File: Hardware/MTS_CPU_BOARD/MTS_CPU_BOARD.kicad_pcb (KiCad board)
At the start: 6 copper layers, 160 x 100 mm, 12 parts, among them J1 DIN41612_02x16_ZB, SW1 SW_DIP_x04, U1 TCAN337GDR, U3 24LC32

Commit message: Add some connectors
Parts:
- added C1: 100n, Capacitor_SMD:C_0402_1005Metric, F.Cu at (118.0, 107.2)
- added D1: Led1, LED_SMD:LED_0805_2012Metric, F.Cu at (198.8, 94.5)
- added J2: THD-02-R, Connector_PinHeader_2.54mm:PinHeader_2x02_P2.54mm_Vertical, F.Cu at (111.7, 108.5)
- added J3: HDMI_A_1.4, Connector_Video:HDMI_A_Kycon_KDMIX-SL1-NS-WS-B15_VerticalRightAngle, F.Cu at (89.9, 95.0)
- added J4: USB3_A_Stacked, Connector_USB:USB3_A_Molex_48406-0001_Horizontal_Stacked, F.Cu at (91.0, 74.0)
- added Module1: ComputeModule4-CM4, CM4IO:Raspberry-Pi-4-Compute-Module, F.Cu at (171.2, 60.0)
- added R1: 680R, Resistor_SMD:R_0805_2012Metric_Pad1.20x1.40mm_HandSolder, F.Cu at (198.9, 91.5)
- added R2: 470R, Resistor_SMD:R_0402_1005Metric, F.Cu at (116.7, 114.3)
- added R3: 470R, Resistor_SMD:R_0402_1005Metric, F.Cu at (116.7, 116.3)
- added S1: SWD, Connector_PinHeader_1.27mm:PinHeader_2x05_P1.27mm_Vertical_SMD, F.Cu at (191.8, 94.2)
- added U2: STM32G431K6Tx, Package_QFP:LQFP-32_7x7mm_P0.8mm, F.Cu at (192.2, 114.9)
- added U4: TPD4EUSB30, Package_SON:USON-10_2.5x1.0mm_P0.5mm, F.Cu at (110.9, 115.6)
- added U5: TPD4EUSB30, Package_SON:USON-10_2.5x1.0mm_P0.5mm, F.Cu at (113.8, 115.6)
- added U6: MagJack-A70-112-331N126, CM4IO:TRJG0926HENL, F.Cu at (90.8, 112.1)
- moved SW1 6.10 mm to (212.2, 114.2), turned to 0 degrees
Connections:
- net /CANH renamed /Conn/CANH
- net /CANL renamed /Conn/CANL
- net /I2C2_CLK_STM_CAN renamed /Conn/I2C2_CLK_STM_CAN
- net /I2C2_SDA_STM_CAN renamed /Conn/I2C2_SDA_STM_CAN
- net /Triger renamed /Conn/Triger

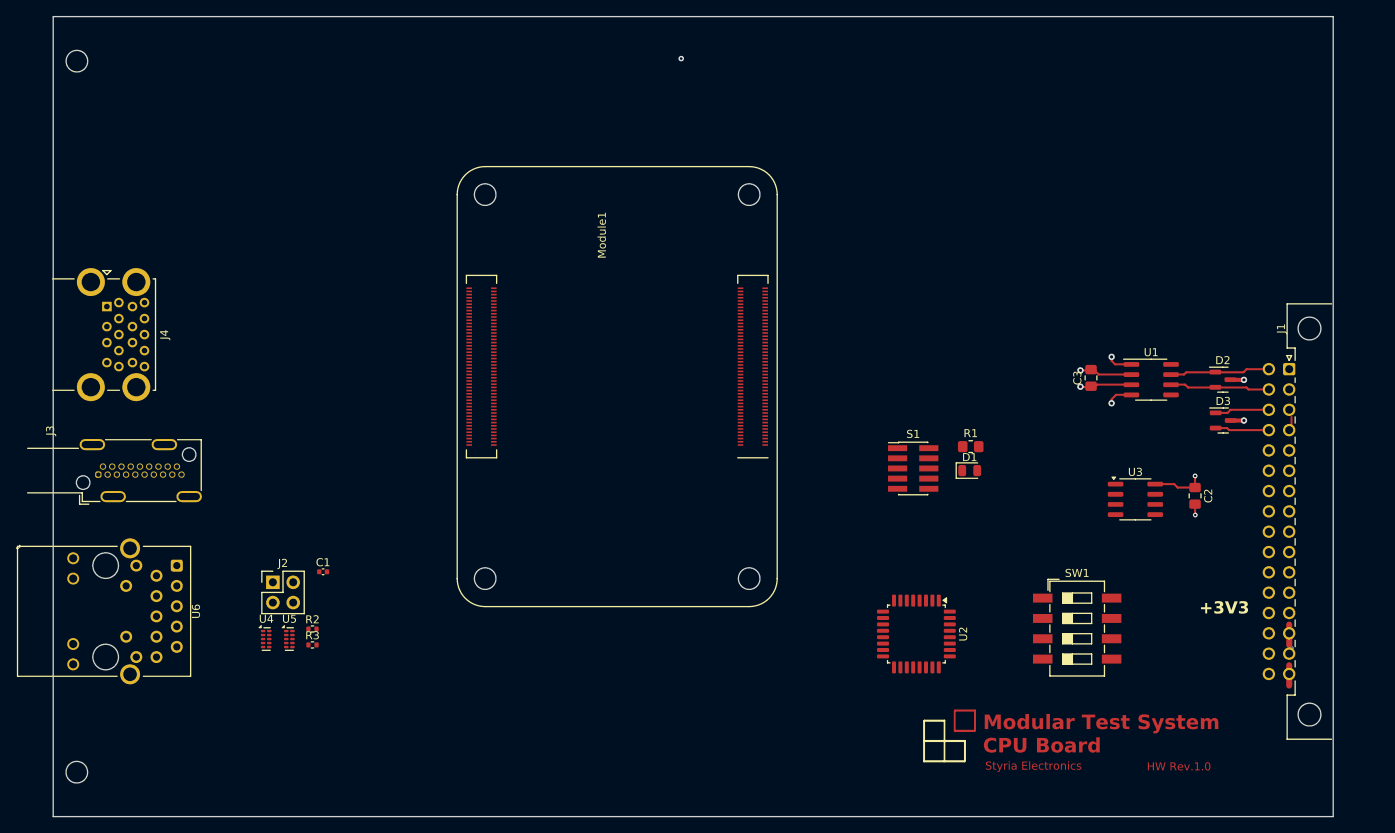
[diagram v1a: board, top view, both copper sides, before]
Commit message: Add EtherCAT
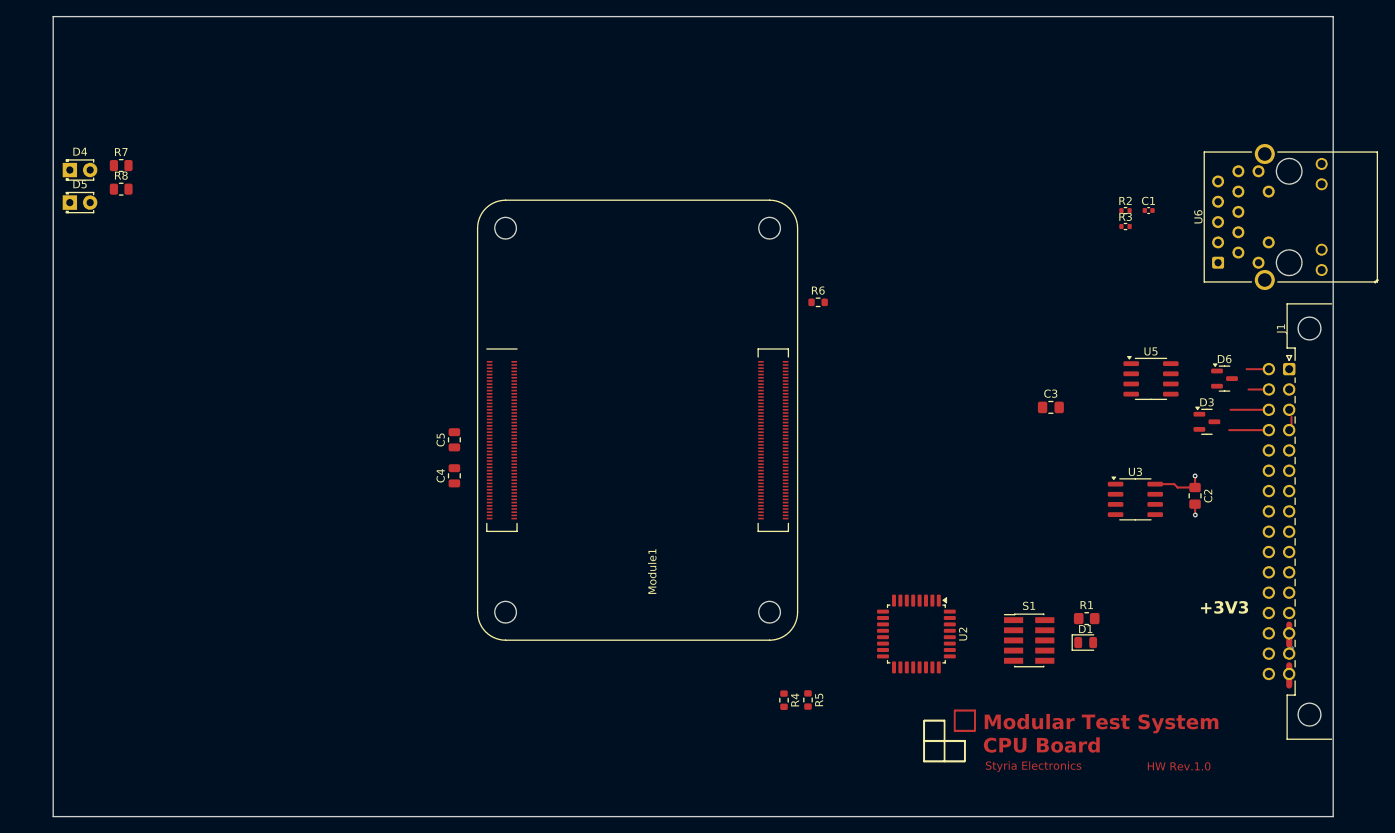
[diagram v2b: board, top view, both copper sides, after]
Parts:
- removed D2: PESD2CANFD24V-T, Package_TO_SOT_SMD:SOT-23
- removed J2: THD-02-R, Connector_PinHeader_2.54mm:PinHeader_2x02_P2.54mm_Vertical
- removed J3: HDMI_A_1.4, Connector_Video:HDMI_A_Kycon_KDMIX-SL1-NS-WS-B15_VerticalRightAngle
- removed J4: USB3_A_Stacked, Connector_USB:USB3_A_Molex_48406-0001_Horizontal_Stacked
- removed MH1, MH3: MountingHole_2.7mm_M2.5_DIN965, MountingHole:MountingHole_2.7mm_M2.5_DIN965
- removed SW1: SW_DIP_x04, Button_Switch_SMD:SW_DIP_SPSTx04_Slide_6.7x11.72mm_W8.61mm_P2.54mm_LowProfile
- removed U1: TCAN337GDR, Package_SO:SOIC-8_3.9x4.9mm_P1.27mm
- removed U4: TPD4EUSB30, Package_SON:USON-10_2.5x1.0mm_P0.5mm
- added C4: 10u, Capacitor_SMD:C_0805_2012Metric, F.Cu at (134.4, 95.2)
- added C5: 10u, Capacitor_SMD:C_0805_2012Metric, F.Cu at (134.4, 90.7)
- added D4: RED, LED_THT:LED_D1.8mm_W3.3mm_H2.4mm, F.Cu at (86.3, 56.9)
- added D5: GREEN, LED_THT:LED_D1.8mm_W3.3mm_H2.4mm, F.Cu at (86.3, 61.0)
- added D6: PESD2CANFD24V-T, Package_TO_SOT_SMD:SOT-23, F.Cu at (230.7, 83.0)
- added R4: 2K2, Resistor_SMD:R_0603_1608Metric, F.Cu at (175.6, 123.2)
- added R5: 2K2, Resistor_SMD:R_0603_1608Metric, F.Cu at (178.6, 123.2)
- added R6: 2.2K, Resistor_SMD:R_0603_1608Metric, F.Cu at (179.9, 73.5)
- added R7: 470R, Resistor_SMD:R_0805_2012Metric, F.Cu at (92.8, 56.4)
- added R8: 470R, Resistor_SMD:R_0805_2012Metric, F.Cu at (92.8, 59.3)
- U5: value TPD4EUSB30 -> TCAN337GDR; footprint Package_SON:USON-10_2.5x1.0mm_P0.5mm -> Package_SO:SOIC-8_3.9x4.9mm_P1.27mm
- moved U6 155.9 mm to (238.8, 62.8), turned to 90 degrees
- moved R2 114.3 mm to (218.3, 62.0)
- moved R3 114.3 mm to (218.3, 64.0)
- moved C1 112.6 mm to (221.2, 62.0)
- moved U5 112.5 mm to (221.5, 83.0)
- moved Module1 60.4 mm to (140.8, 112.2), turned to 0 degrees
- moved D1 25.9 mm to (213.3, 116.0)
- moved R1 25.9 mm to (213.4, 113.0)
- moved S1 25.9 mm to (206.2, 115.7)
- moved C3 6.23 mm to (209.0, 86.6), turned to 0 degrees
- moved D3 2.04 mm to (228.5, 88.4)
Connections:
- J1 pad b1: /Conn/CANH -> /STM32/CANH
- J1 pad b10: b10 -> /CM4/TRD1_N
- J1 pad b2: /Conn/CANL -> /STM32/CANL
- J1 pad b7: b7 -> /CM4/TRD0_P
- J1 pad b8: b8 -> /CM4/TRD0_N
- J1 pad b9: b9 -> /CM4/TRD1_P
- Module1 pad 1: unconnected-(Module1A-GND-Pad1) -> GND
- Module1 pad 10: unconnected-(Module1A-Ethernet_Pair0_N-Pad10) -> /CM4/TRD0_N
- Module1 pad 101: unconnected-(Module1B-USB_OTG_ID-Pad101) -> Net-(Module1B-USB_OTG_ID)
- Module1 pad 103: unconnected-(Module1B-USB2_N-Pad103) -> /CM4/USBD_N
- Module1 pad 105: unconnected-(Module1B-USB2_P-Pad105) -> /CM4/USBD_P
- Module1 pad 107: unconnected-(Module1B-GND-Pad107) -> GND
- Module1 pad 108: unconnected-(Module1B-GND-Pad108) -> GND
- Module1 pad 113: unconnected-(Module1B-GND-Pad113) -> GND
- Module1 pad 114: unconnected-(Module1B-GND-Pad114) -> GND
- Module1 pad 119: unconnected-(Module1B-GND-Pad119) -> GND
- Module1 pad 12: unconnected-(Module1A-Ethernet_Pair0_P-Pad12) -> /CM4/TRD0_P
- Module1 pad 120: unconnected-(Module1B-GND-Pad120) -> GND
- Module1 pad 125: unconnected-(Module1B-GND-Pad125) -> GND
- Module1 pad 126: unconnected-(Module1B-GND-Pad126) -> GND
- Module1 pad 13: unconnected-(Module1A-GND-Pad13) -> GND
- Module1 pad 131: unconnected-(Module1B-GND-Pad131) -> GND
- Module1 pad 132: unconnected-(Module1B-GND-Pad132) -> GND
- Module1 pad 137: unconnected-(Module1B-GND-Pad137) -> GND
- Module1 pad 138: unconnected-(Module1B-GND-Pad138) -> GND
- Module1 pad 14: unconnected-(Module1A-GND-Pad14) -> GND
- Module1 pad 144: unconnected-(Module1B-GND-Pad144) -> GND
- Module1 pad 15: unconnected-(Module1A-Ethernet_nLED3(3.3v)-Pad15) -> /CM4/ETH_LEDY
- Module1 pad 150: unconnected-(Module1B-GND-Pad150) -> GND
- Module1 pad 155: unconnected-(Module1B-GND-Pad155) -> GND
- Module1 pad 156: unconnected-(Module1B-GND-Pad156) -> GND
- Module1 pad 161: unconnected-(Module1B-GND-Pad161) -> GND
- Module1 pad 162: unconnected-(Module1B-GND-Pad162) -> GND
- Module1 pad 167: unconnected-(Module1B-GND-Pad167) -> GND
- Module1 pad 168: unconnected-(Module1B-GND-Pad168) -> GND
- Module1 pad 17: unconnected-(Module1A-Ethernet_nLED2(3.3v)-Pad17) -> /CM4/ETH_LEDG
- Module1 pad 173: unconnected-(Module1B-GND-Pad173) -> GND
- Module1 pad 174: unconnected-(Module1B-GND-Pad174) -> GND
- Module1 pad 179: unconnected-(Module1B-GND-Pad179) -> GND
- Module1 pad 180: unconnected-(Module1B-GND-Pad180) -> GND
- Module1 pad 185: unconnected-(Module1B-GND-Pad185) -> GND
- Module1 pad 186: unconnected-(Module1B-GND-Pad186) -> GND
- Module1 pad 19: unconnected-(Module1A-Ethernet_nLED1(3.3v)-Pad19) -> /CM4/ETH_LEDO
- Module1 pad 191: unconnected-(Module1B-GND-Pad191) -> GND
- Module1 pad 192: unconnected-(Module1B-GND-Pad192) -> GND
- Module1 pad 197: unconnected-(Module1B-GND-Pad197) -> GND
- Module1 pad 198: unconnected-(Module1B-GND-Pad198) -> GND
- Module1 pad 2: unconnected-(Module1A-GND-Pad2) -> GND
- Module1 pad 21: unconnected-(Module1A-PI_nLED_Activity-Pad21) -> /CM4/SSD_LED
- Module1 pad 22: unconnected-(Module1A-GND-Pad22) -> GND
- Module1 pad 23: unconnected-(Module1A-GND-Pad23) -> GND
- Module1 pad 32: unconnected-(Module1A-GND-Pad32) -> GND
- Module1 pad 33: unconnected-(Module1A-GND-Pad33) -> GND
- Module1 pad 35: unconnected-(Module1A-ID_SC-Pad35) -> /CM4/USART2_RX
- Module1 pad 4: unconnected-(Module1A-Ethernet_Pair1_P-Pad4) -> /CM4/TRD1_P
- Module1 pad 42: unconnected-(Module1A-GND-Pad42) -> GND
- Module1 pad 43: unconnected-(Module1A-GND-Pad43) -> GND
- Module1 pad 45: unconnected-(Module1A-GPIO24-Pad45) -> BUSSY LED
- Module1 pad 47: unconnected-(Module1A-GPIO23-Pad47) -> Error LED
- Module1 pad 50: unconnected-(Module1A-GPIO17-Pad50) -> /CM4/STM_RESET
- Module1 pad 51: unconnected-(Module1A-GPIO15-Pad51) -> USART1_RX
- Module1 pad 52: unconnected-(Module1A-GND-Pad52) -> GND
- Module1 pad 53: unconnected-(Module1A-GND-Pad53) -> GND
- Module1 pad 54: unconnected-(Module1A-GPIO4-Pad54) -> /CM4/Triger
- Module1 pad 55: unconnected-(Module1A-GPIO14-Pad55) -> USART1_TX
- Module1 pad 56: unconnected-(Module1A-GPIO3-Pad56) -> /CM4/I2C_CLK_CM4
- Module1 pad 58: unconnected-(Module1A-GPIO2-Pad58) -> /CM4/I2C_SDA_CM4
- Module1 pad 59: unconnected-(Module1A-GND-Pad59) -> GND
- Module1 pad 6: unconnected-(Module1A-Ethernet_Pair1_N-Pad6) -> /CM4/TRD1_N
- Module1 pad 60: unconnected-(Module1A-GND-Pad60) -> GND
- Module1 pad 65: unconnected-(Module1A-GND-Pad65) -> GND
- Module1 pad 66: unconnected-(Module1A-GND-Pad66) -> GND
- Module1 pad 7: unconnected-(Module1A-GND-Pad7) -> GND
- Module1 pad 71: unconnected-(Module1A-GND-Pad71) -> GND
- Module1 pad 74: unconnected-(Module1A-GND-Pad74) -> GND
- Module1 pad 77: unconnected-(Module1A-+5v_(Input)-Pad77) -> +5V
- Module1 pad 78: unconnected-(Module1A-GPIO_VREF(1.8v/3.3v_Input)-Pad78) -> +3V3
- Module1 pad 79: unconnected-(Module1A-+5v_(Input)-Pad79) -> +5V
- Module1 pad 8: unconnected-(Module1A-GND-Pad8) -> GND
- Module1 pad 81: unconnected-(Module1A-+5v_(Input)-Pad81) -> +5V
- Module1 pad 83: unconnected-(Module1A-+5v_(Input)-Pad83) -> +5V
- Module1 pad 85: unconnected-(Module1A-+5v_(Input)-Pad85) -> +5V
- Module1 pad 87: unconnected-(Module1A-+5v_(Input)-Pad87) -> +5V
- Module1 pad 95: unconnected-(Module1A-nPI_LED_PWR-Pad95) -> PWR LED
- Module1 pad 98: unconnected-(Module1A-GND-Pad98) -> GND
- R2 pad 2: /Ethernet/ETH_LEDG -> unconnected-(R2-Pad2)
- R3 pad 2: /Ethernet/ETH_LEDY -> unconnected-(R3-Pad2)
- U5 pad 1: /Ethernet/TRD1_P -> CANFD_TX
- U5 pad 2: /Ethernet/TRD1_N -> GND
- U5 pad 3: GND -> +3V3
- U5 pad 4: /Ethernet/TRD0_N -> CANFD_RX
- U5 pad 5: /Ethernet/TRD0_P -> unconnected-(U5-VIO-Pad5)
- U5 pad 6: /Ethernet/TRD0_P -> /STM32/CANL
- U5 pad 7: /Ethernet/TRD0_N -> /STM32/CANH
- U5 pad 8: GND -> unconnected-(U5-STB-Pad8)
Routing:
- net /Conn/CANH: track 13.2 -> 0.00 mm
- net /Conn/CANL: track 13.1 -> 0.00 mm
- net GND: track 11.0 -> 1.37 mm, vias 4 -> 1
- net +3V3: track 12.5 -> 6.61 mm, vias 2 -> 1
- net /STM32/CANH: track 0.00 -> 2.79 mm
- net CANFD_RX: track 2.56 -> 0.00 mm, vias 1 -> 0
- net /STM32/CANL: track 0.00 -> 2.55 mm
- net CANFD_TX: track 2.50 -> 0.00 mm, vias 1 -> 0
- net I2C_BUS_SDA: track 6.83 -> 4.80 mm
- net I2C_BUS_CLK: track 6.75 -> 4.97 mm
- net (no net): vias 1 -> 0
